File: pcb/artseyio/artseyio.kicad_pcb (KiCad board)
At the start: 2 copper layers, 95.2 x 69.9 mm, 17 parts, among them J1 USB_C16PIN, SW1 SW_MEC_5G, SW2 SW_MEC_5G, SW3 SW_MEC_5G, SW4 SW_MEC_5G, SW5 SW_MEC_5G, SW6 SW_MEC_5G, SW7 SW_MEC_5G, SW8 SW_MEC_5G, U1 RP2040-Zero, U2 mini_esp32, U3 CH552G

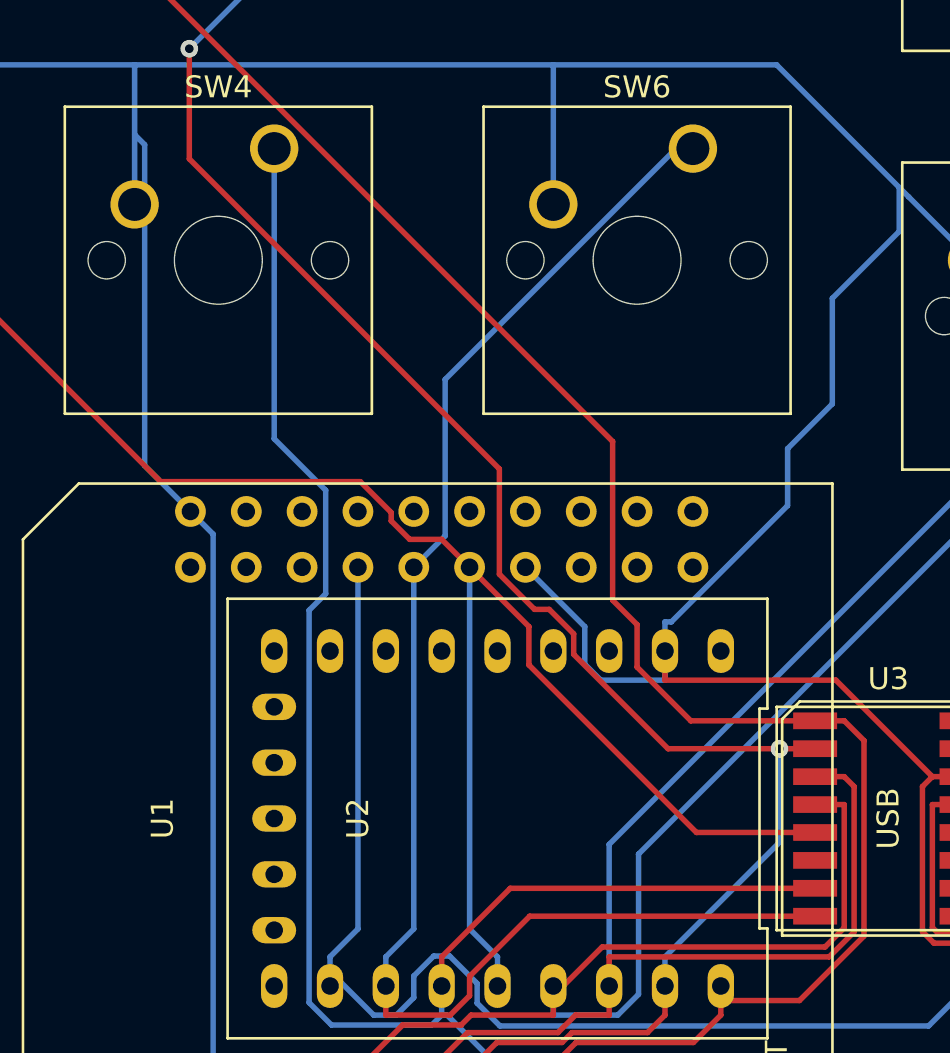
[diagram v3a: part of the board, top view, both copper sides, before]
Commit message: Added reset jumpers for CH552G
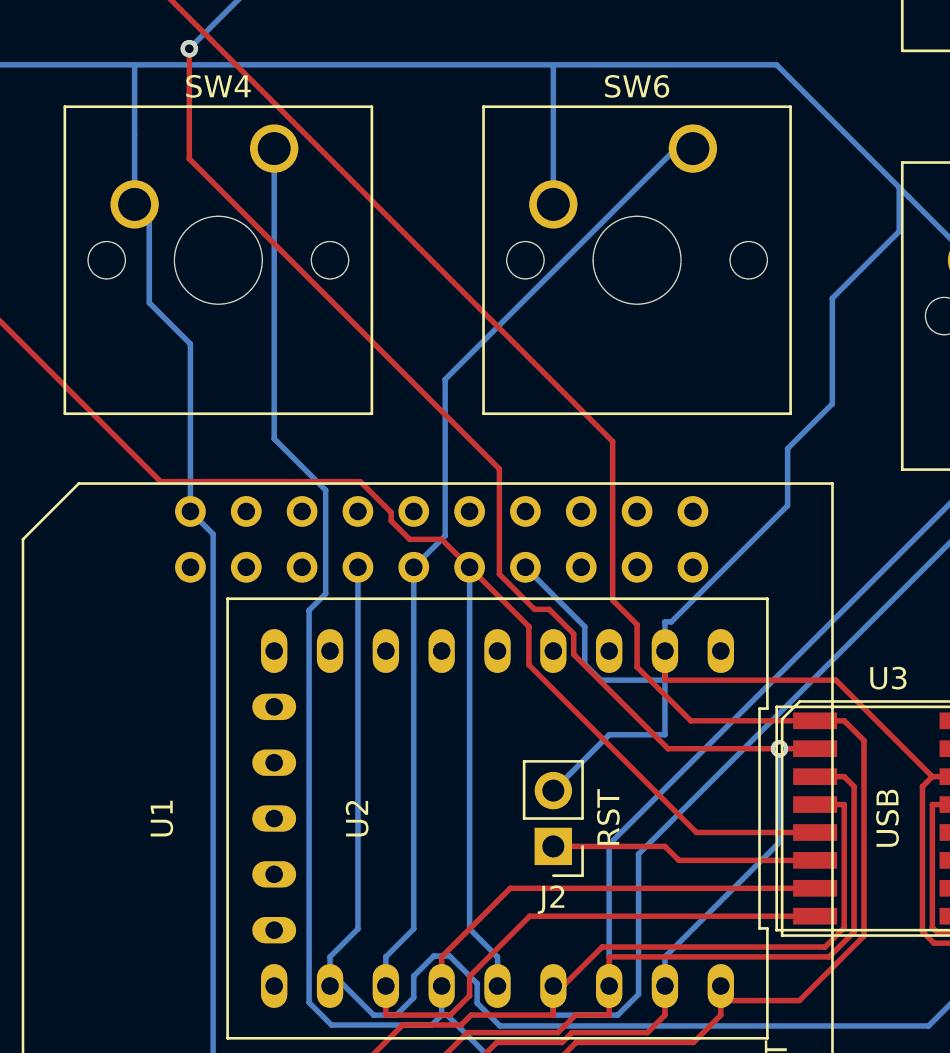
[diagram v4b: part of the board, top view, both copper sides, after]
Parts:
- added J2: RST, Connector_PinHeader_2.54mm:PinHeader_1x02_P2.54mm_Vertical, F.Cu at (160.0, 119.4)
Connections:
- U3 pad 6: unconnected-(U3-Pad6) -> Net-(U3-Pad6)
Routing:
- net Net-(U3-Pad6): track 0.00 -> 12.2 mm
- net Earth: track 296.4 -> 303.2 mm
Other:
- board text added: "RST"
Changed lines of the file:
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@@
   (net 57 "Net-(J1-PadA7)")
   (net 58 "unconnected-(J1-PadB5)")
-  (net 59 "unconnected-(U3-Pad6)")
+  (net 59 "Net-(U3-Pad6)")
   (net 60 "unconnected-(U3-Pad10)")
   (net 61 "unconnected-(U3-Pad11)")
@@
       (net 2 "/E") (pinfunction "P1.7") (pintype "bidirectional"))
     (pad "6" smd rect (at 1.905 3.33 270) (size 0.76 2) (layers "F.Cu" "F.Paste" "F.Mask")
-      (net 59 "unconnected-(U3-Pad6)") (pinfunction "RST") (pintype "bidirectional"))
+      (net 59 "Net-(U3-Pad6)") (pinfunction "RST") (pintype "bidirectional"))
     (pad "7" smd rect (at 3.175 3.33 270) (size 0.76 2) (layers "F.Cu" "F.Paste" "F.Mask")
       (net 4 "/Y") (pinfunction "P3.1") (pintype "bidirectional"))
@@
     (fp_circle (center 0 0) (end 3.45 0) (layer "F.CrtYd") (width 0.05) (fill none))
     (pad "" np_thru_hole circle (at 0 0) (size 3.2 3.2) (drill 3.2) (layers *.Cu *.Mask))
+  )
+  (footprint "Connector_PinHeader_2.54mm:PinHeader_1x02_P2.54mm_Vertical" (layer "F.Cu")
+    (at 160.02 119.38 180)
+    (descr "Through hole straight pin header, 1x02, 2.54mm pitch, single row")
+    (tags "Through hole pin header THT 1x02 2.54mm single row")
+    (property "Sheetfile" "artseyio.kicad_sch")
+    (property "Sheetname" "")
+    (attr through_hole)
+    (fp_text reference "J2" (at 0 -2.33) (layer "F.SilkS")
+      (effects (font (size 1 1) (thickness 0.15)))
+    )
+    (fp_text value "RST" (at 0 4.87) (layer "F.Fab")
+      (effects (font (size 1 1) (thickness 0.15)))
+    )
+    (fp_text user "${REFERENCE}" (at 0 1.27 90) (layer "F.Fab")
+      (effects (font (size 1 1) (thickness 0.15)))
+    )
+    (fp_line (start -1.33 0) (end -1.33 -1.33) (layer "F.SilkS") (width 0.12))
+    (fp_line (start -1.33 1.27) (end 1.33 1.27) (layer "F.SilkS") (width 0.12))
+    (fp_line (start -1.33 1.27) (end -1.33 3.87) (layer "F.SilkS") (width 0.12))
+    (fp_line (start -1.33 -1.33) (end 0 -1.33) (layer "F.SilkS") (width 0.12))
+    (fp_line (start 1.33 1.27) (end 1.33 3.87) (layer "F.SilkS") (width 0.12))
+    (fp_line (start -1.33 3.87) (end 1.33 3.87) (layer "F.SilkS") (width 0.12))
+    (fp_line (start 1.8 -1.8) (end -1.8 -1.8) (layer "F.CrtYd") (width 0.05))
+    (fp_line (start 1.8 4.35) (end 1.8 -1.8) (layer "F.CrtYd") (width 0.05))
+    (fp_line (start -1.8 4.35) (end 1.8 4.35) (layer "F.CrtYd") (width 0.05))
+    (fp_line (start -1.8 -1.8) (end -1.8 4.35) (layer "F.CrtYd") (width 0.05))
+    (fp_line (start 1.27 3.81) (end -1.27 3.81) (layer "F.Fab") (width 0.1))
+    (fp_line (start -1.27 3.81) (end -1.27 -0.635) (layer "F.Fab") (width 0.1))
+    (fp_line (start -0.635 -1.27) (end 1.27 -1.27) (layer "F.Fab") (width 0.1))
+    (fp_line (start 1.27 -1.27) (end 1.27 3.81) (layer "F.Fab") (width 0.1))
+    (fp_line (start -1.27 -0.635) (end -0.635 -1.27) (layer "F.Fab") (width 0.1))
+    (pad "1" thru_hole rect (at 0 0 180) (size 1.7 1.7) (drill 1) (layers *.Cu *.Mask)
+      (net 59 "Net-(U3-Pad6)") (pinfunction "Pin_1") (pintype "passive"))
+    (pad "2" thru_hole oval (at 0 2.54 180) (size 1.7 1.7) (drill 1) (layers *.Cu *.Mask)
+      (net 23 "Earth") (pinfunction "Pin_2") (pintype "passive"))
+    (model "${KICAD6_3DMODEL_DIR}/Connector_PinHeader_2.54mm.3dshapes/PinHeader_1x02_P2.54mm_Vertical.wrl"
+      (offset (xyz 0 0 0))
+      (scale (xyz 1 1 1))
+      (rotate (xyz 0 0 0))
+    )
   )
   (footprint "Button_Switch_Keyboard:SW_Cherry_MX_1.00u_PCB" (layer "F.Cu")
@@
   (gr_text "ARTS\nEYIO" (at 127 115.57) (layer "F.SilkS")
     (effects (font (size 3 3) (thickness 0.15)))
+  )
+  (gr_text "RST" (at 162.56 118.11 90) (layer "F.SilkS")
+    (effects (font (size 1 1) (thickness 0.15)))
   )
   (segment (start 167.64 127.0551) (end 166.3942 128.3009) (width 0.25) (layer "F.Cu") (net 1))
@@
   (segment (start 182.0643 116.205) (end 178.59 116.205) (width 0.25) (layer "F.Cu") (net 23))
   (segment (start 165.1 110.49) (end 165.1 111.8151) (width 0.25) (layer "B.Cu") (net 23))
-  (segment (start 141.4268 102.0568) (end 143.51 104.14) (width 0.25) (layer "B.Cu") (net 23))
   (segment (start 161.4493 111.089) (end 161.4493 109.3793) (width 0.25) (layer "B.Cu") (net 23))
   (segment (start 175.7577 89.3975) (end 175.7577 91.3995) (width 0.25) (layer "B.Cu") (net 23))
   (segment (start 165.3875 109.1649) (end 165.1 109.1649) (width 0.25) (layer "B.Cu") (net 23))
+  (segment (start 165.1 114.3) (end 165.1 110.49) (width 0.25) (layer "B.Cu") (net 23))
   (segment locked (start 121.92 83.82) (end 121.92 72.39) (width 0.25) (layer "B.Cu") (net 23))
   (segment locked (start 121.92 91.44) (end 121.92 83.82) (width 0.25) (layer "B.Cu") (net 23))
   (segment (start 165.1 110.49) (end 165.1 109.1649) (width 0.25) (layer "B.Cu") (net 23))
   (segment locked (start 121.92 83.82) (end 140.97 83.82) (width 0.25) (layer "B.Cu") (net 23))
+  (segment (start 160.02 116.84) (end 162.56 114.3) (width 0.25) (layer "B.Cu") (net 23))
   (segment locked (start 140.97 66.04) (end 160.02 66.04) (width 0.25) (layer "B.Cu") (net 23))
   (segment locked (start 160.02 90.17) (end 160.02 83.82) (width 0.25) (layer "B.Cu") (net 23))
@@
   (segment locked (start 140.97 86.995) (end 140.97 83.82) (width 0.25) (layer "B.Cu") (net 23))
   (segment locked (start 160.02 66.04) (end 171.45 66.04) (width 0.25) (layer "B.Cu") (net 23))
-  (segment (start 141.4268 87.4518) (end 141.4268 102.0568) (width 0.25) (layer "B.Cu") (net 23))
   (segment (start 161.4493 109.3793) (end 158.75 106.68) (width 0.25) (layer "B.Cu") (net 23))
   (segment locked (start 160.02 71.12) (end 160.02 66.04) (width 0.25) (layer "B.Cu") (net 23))
@@
   (segment locked (start 160.02 83.82) (end 170.18 83.82) (width 0.25) (layer "B.Cu") (net 23))
   (segment (start 162.1754 111.8151) (end 161.4493 111.089) (width 0.25) (layer "B.Cu") (net 23))
+  (segment (start 162.56 114.3) (end 165.1 114.3) (width 0.25) (layer "B.Cu") (net 23))
+  (segment (start 143.51 104.14) (end 143.51 96.52) (width 0.25) (layer "B.Cu") (net 23))
   (segment (start 144.5419 131.0481) (end 144.5419 105.1719) (width 0.25) (layer "B.Cu") (net 23))
   (segment locked (start 123.19 66.04) (end 140.97 66.04) (width 0.25) (layer "B.Cu") (net 23))
   (segment (start 175.7577 91.3995) (end 172.7129 94.4443) (width 0.25) (layer "B.Cu") (net 23))
+  (segment (start 143.51 96.52) (end 141.637383 94.647383) (width 0.25) (layer "B.Cu") (net 23))
   (segment locked (start 140.97 83.82) (end 160.02 83.82) (width 0.25) (layer "B.Cu") (net 23))
   (segment locked (start 121.92 67.31) (end 123.19 66.04) (width 0.25) (layer "B.Cu") (net 23))
   (segment (start 143.51 132.08) (end 144.5419 131.0481) (width 0.25) (layer "B.Cu") (net 23))
   (segment locked (start 140.97 71.12) (end 140.97 66.04) (width 0.25) (layer "B.Cu") (net 23))
+  (segment (start 141.637383 94.647383) (end 141.637383 90.837383) (width 0.25) (layer "B.Cu") (net 23))
   (segment (start 172.7129 94.4443) (end 172.7129 99.247) (width 0.25) (layer "B.Cu") (net 23))
   (segment (start 165.1 111.8151) (end 162.1754 111.8151) (width 0.25) (layer "B.Cu") (net 23))
   (segment (start 172.7129 99.247) (end 170.6773 101.2826) (width 0.25) (layer "B.Cu") (net 23))
+  (segment (start 141.637383 90.837383) (end 140.97 90.17) (width 0.25) (layer "B.Cu") (net 23))
   (segment (start 170.6773 103.8751) (end 165.3875 109.1649) (width 0.25) (layer "B.Cu") (net 23))
-  (segment (start 140.97 86.995) (end 141.4268 87.4518) (width 0.25) (layer "B.Cu") (net 23))
   (segment (start 184.4344 120.56) (end 185.1118 120.56) (width 0.25) (layer "F.Cu") (net 29))
   (segment (start 185.1118 120.56) (end 185.9956 119.6762) (width 0.25) (layer "F.Cu") (net 29))
@@
   (segment (start 178.59 117.475) (end 177.2649 117.475) (width 0.25) (layer "F.Cu") (net 57))
   (segment (start 182.83 119.4143) (end 183.3843 118.86) (width 0.25) (layer "F.Cu") (net 57))
+  (segment (start 160.02 119.38) (end 165.1 119.38) (width 0.25) (layer "F.Cu") (net 59))
+  (segment (start 165.735 120.015) (end 165.1 119.38) (width 0.25) (layer "F.Cu") (net 59))
+  (segment (start 171.93 120.015) (end 165.735 120.015) (width 0.25) (layer "F.Cu") (net 59))
 )

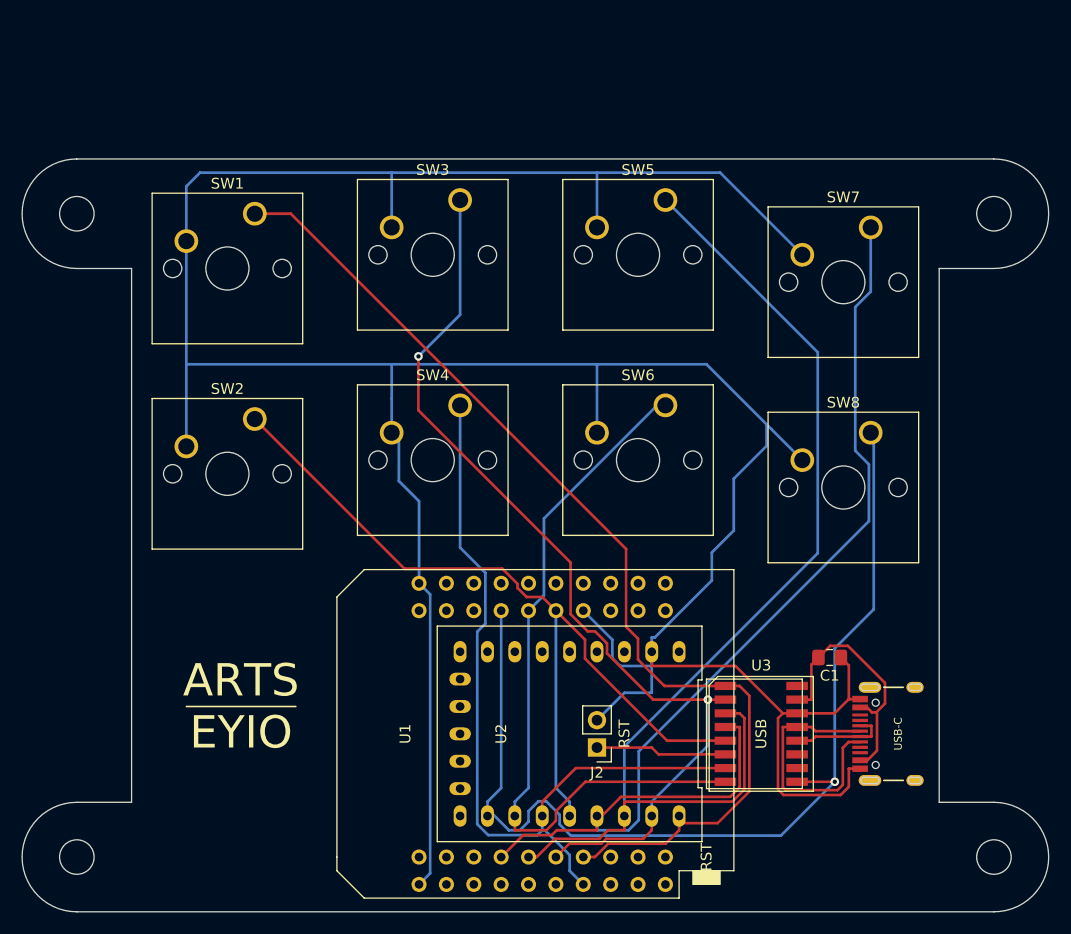
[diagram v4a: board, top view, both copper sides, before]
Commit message: Updated to remove RP2040-Zero and ESP32.
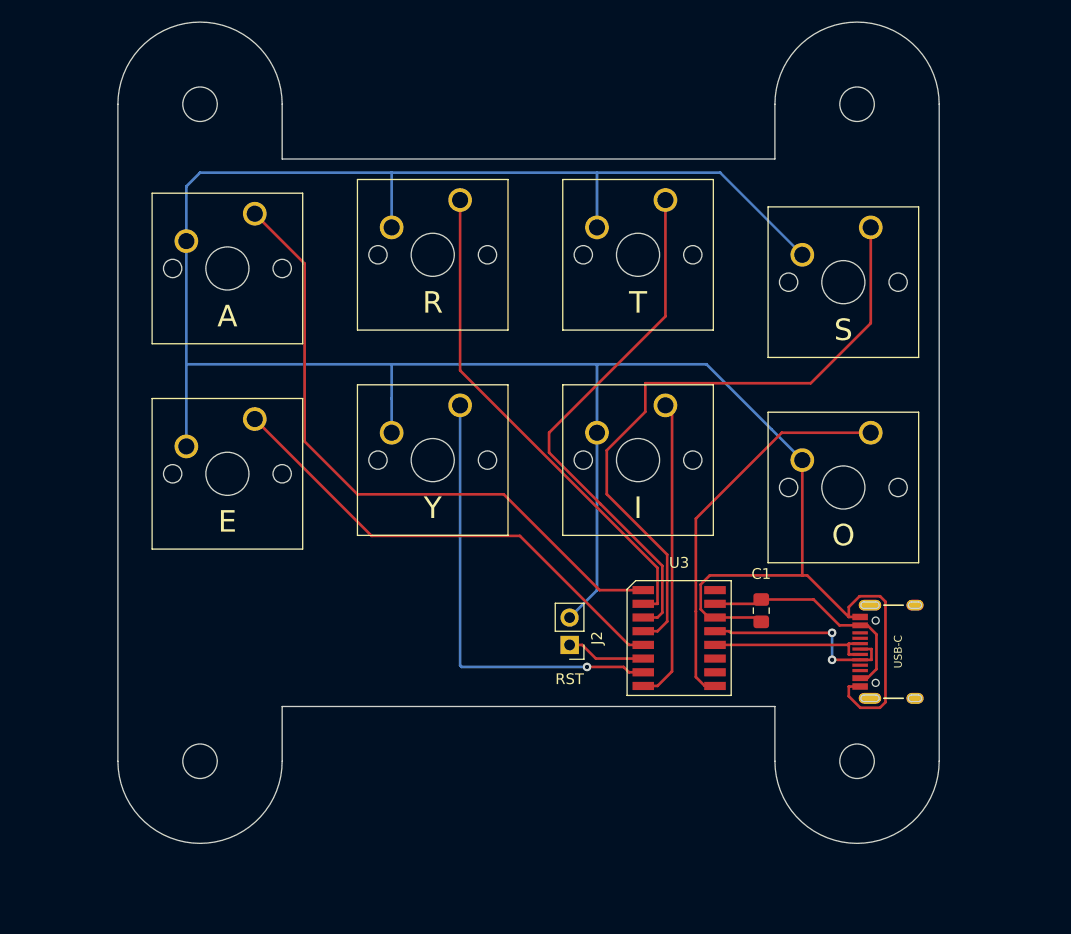
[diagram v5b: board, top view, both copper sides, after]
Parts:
- removed U1: RP2040-Zero, Andrews-Custom:RP2040-Zero
- removed U2: mini_esp32, ESP32 Mini:ESP32_mini
- moved H3 16.3 mm to (184.2, 59.7)
- moved H4 15.5 mm to (184.2, 120.7)
- moved H1 15.3 mm to (123.2, 59.7)
- moved H2 14.5 mm to (123.2, 120.7)
- moved U3 11.7 mm to (167.6, 109.2)
- moved J2 9.85 mm to (157.5, 109.9)
- moved C1 7.69 mm to (175.3, 106.7), turned to 90 degrees
- moved J1 7.62 mm to (184.4, 110.5)
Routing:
- net Earth: track 303.2 -> 243.0 mm
- net /O: track 95.7 -> 36.3 mm, vias 1 -> 0
- net /T: track 103.2 -> 49.1 mm
- net /R: track 88.3 -> 46.4 mm, vias 2 -> 0
- net /S: track 103.2 -> 61.4 mm
- net /I: track 67.6 -> 28.2 mm
- net /A: track 97.6 -> 60.2 mm
- net /Y: track 74.5 -> 41.4 mm, vias 0 -> 1
- net /E: track 76.8 -> 44.7 mm
- net Net-(J1-PadA6): track 9.10 -> 15.5 mm
- net Net-(J1-PadA7): track 24.1 -> 19.1 mm, vias 0 -> 2
- net Net-(J2-Pad1): track 12.2 -> 7.35 mm
- net Net-(C1-Pad2): track 23.8 -> 21.6 mm
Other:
- board size 95.2 x 69.9 mm -> 76.2 x 76.2 mm
- board text added: "A"
- board text added: "E"
- board text added: "I"
- board text added: "O"
- board text added: "R"
- board text added: "S"
- board text added: "T"
- board text added: "Y"
- board text removed: "ARTS EYIO"

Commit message: Added in some missing features to make programming it easier, handle CC lines on USB-C.
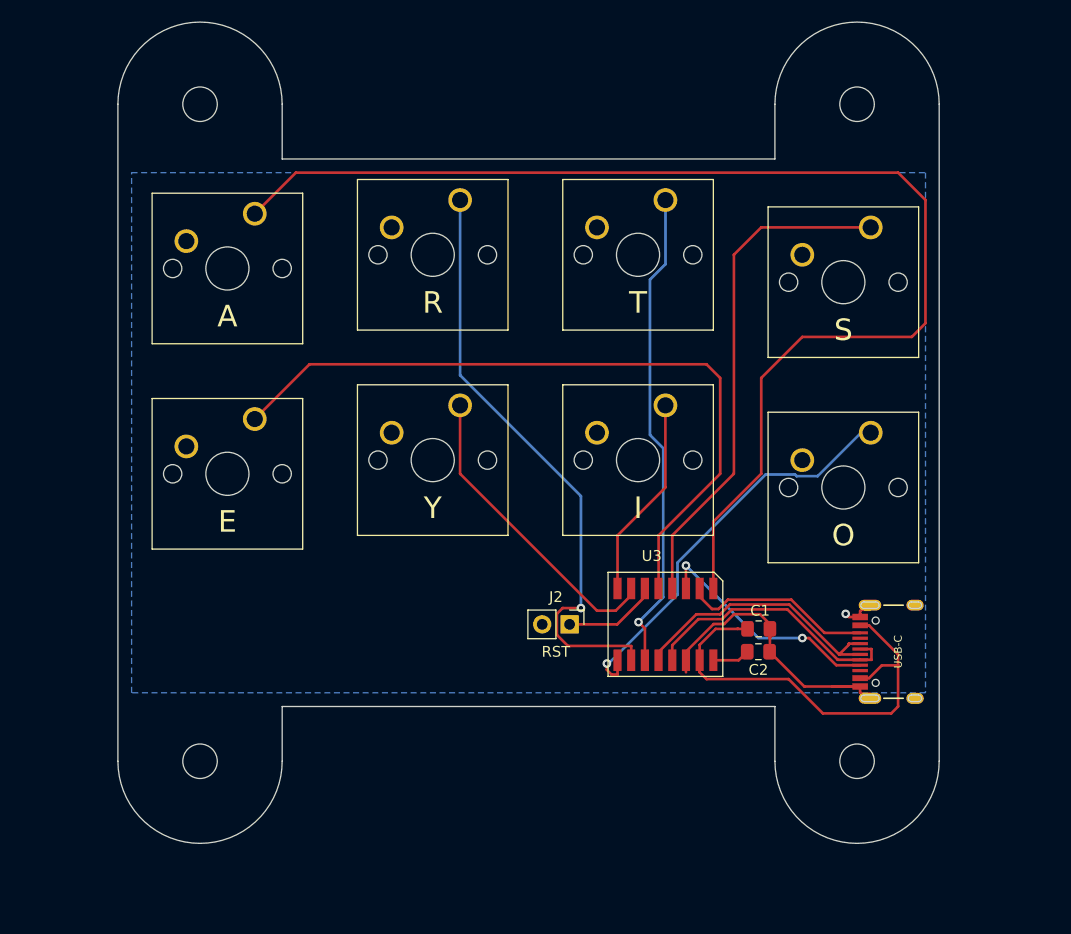
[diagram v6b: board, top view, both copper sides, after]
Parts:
- added C2: 0.1uF, Capacitor_SMD:C_0805_2012Metric_Pad1.18x1.45mm_HandSolder, F.Cu at (175.0, 110.5)
- moved J2 1.91 mm to (157.5, 108.0), turned to -90 degrees
- moved U3 1.80 mm to (166.4, 108.0), turned to 180 degrees
- moved C1 1.70 mm to (175.0, 108.4), turned to 180 degrees
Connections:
- J1 pad A5: unconnected-(J1-PadA5) -> /CC2
- J1 pad B5: unconnected-(J1-PadB5) -> /CC1
- J1 pad SHLD1: Net-(J1-PadSHLD1) -> Earth
- J1 pad SHLD2: Net-(J1-PadSHLD1) -> Earth
- J1 pad SHLD3: Net-(J1-PadSHLD1) -> Earth
- J1 pad SHLD4: Net-(J1-PadSHLD1) -> Earth
- J1 pad SHLD5: Net-(J1-PadSHLD1) -> Earth
- J1 pad SHLD6: Net-(J1-PadSHLD1) -> Earth
- J1 pad SHLD7: Net-(J1-PadSHLD1) -> Earth
- J1 pad SHLD8: Net-(J1-PadSHLD1) -> Earth
- U3 pad 10: unconnected-(U3-Pad10) -> /R
- U3 pad 11: unconnected-(U3-Pad11) -> /T
- U3 pad 16: unconnected-(U3-Pad16) -> Net-(U3-Pad16)
- U3 pad 2: /R -> /CC1
- U3 pad 3: /T -> /CC2
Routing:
- net Earth: track 243.0 -> 32.0 mm, vias 0 -> 1
- net /A: track 60.2 -> 115.0 mm
- net /E: track 44.7 -> 67.7 mm
- net /CC2: track 0.00 -> 22.1 mm, vias 0 -> 2
- net Net-(C1-Pad2): track 21.6 -> 41.4 mm
- net /CC1: track 0.00 -> 18.4 mm
- net /S: track 61.4 -> 47.1 mm
- net /Y: track 41.4 -> 28.7 mm, vias 1 -> 0
- net Net-(J1-PadA6): track 15.5 -> 25.6 mm
- net /I: track 28.2 -> 18.8 mm
- net /R: track 46.4 -> 55.6 mm, vias 0 -> 1
- net Net-(J1-PadA7): track 19.1 -> 25.2 mm, vias 2 -> 0
- net /T: track 49.1 -> 45.0 mm, vias 0 -> 1
- net Net-(U3-Pad16): track 0.00 -> 4.03 mm
- net /O: track 36.3 -> 38.3 mm, vias 0 -> 1
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- added copper zone on B.Cu, net Earth
